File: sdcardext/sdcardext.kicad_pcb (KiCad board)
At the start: 2 copper layers, 2 parts, among them J1 Micro_SD_Card_Det2

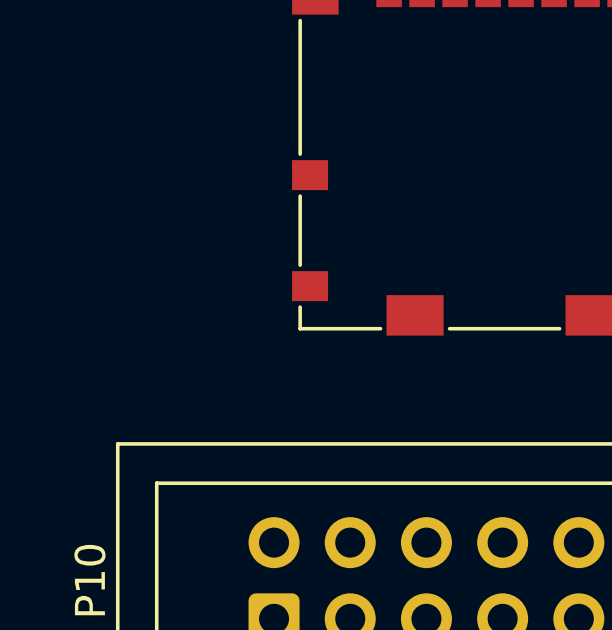
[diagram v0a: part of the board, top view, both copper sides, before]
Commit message: add part#, pullup for CD
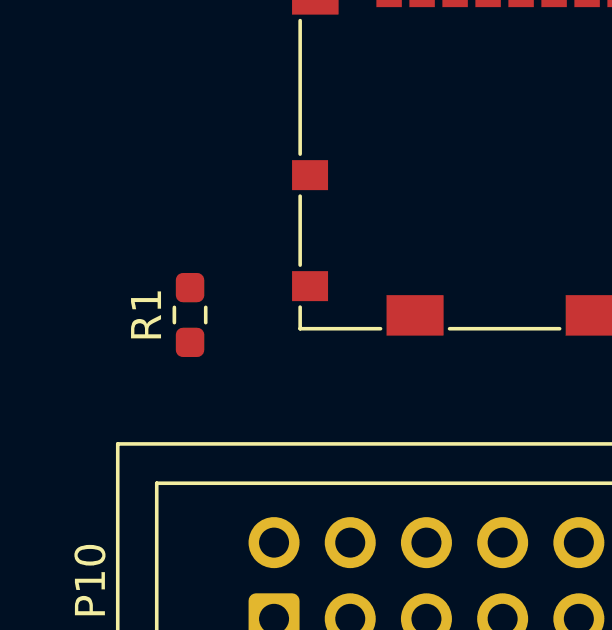
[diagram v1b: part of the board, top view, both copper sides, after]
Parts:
- added R1: 10k, Resistor_SMD:R_0603_1608Metric_Pad0.98x0.95mm_HandSolder, F.Cu at (90.5, 70.7)
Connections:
- J1 pad 10: unconnected-(J1-DET_A-Pad10) -> Net-(J1-DET_A)
- J1 pad 9: unconnected-(J1-DET_B-Pad9) -> Net-(J1-DET_A)
- P10 pad 6: unconnected-(P10-CD-Pad6) -> Net-(J1-DET_A)
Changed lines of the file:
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@@
 	(net 1 "Net-(J1-CMD)")
 	(net 2 "Net-(J1-DAT1)")
-	(net 3 "unconnected-(J1-DET_B-Pad9)")
+	(net 3 "Net-(J1-DET_A)")
 	(net 4 "Net-(J1-CLK)")
 	(net 5 "Net-(J1-DAT3{slash}CD)")
@@
 	(net 8 "VCC")
 	(net 9 "Net-(J1-DAT2)")
-	(net 10 "unconnected-(P10-CD-Pad6)")
-	(net 11 "unconnected-(J1-SHIELD-Pad11)")
-	(net 12 "unconnected-(J1-DET_A-Pad10)")
+	(net 10 "unconnected-(J1-SHIELD-Pad11)")
 	(footprint "Connector_Card:microSD_HC_Molex_104031-0811"
 		(layer "F.Cu")
@@
 			)
 		)
+		(property "LCSC" "C585350"
+			(at 0 0 0)
+			(layer "F.SilkS")
+			(hide yes)
+			(effects
+				(font
+					(size 1.27 1.27)
+					(thickness 0.15)
+				)
+			)
+		)
 		(property ki_fp_filters "microSD*")
 		(sheetname "/")
@@
 			(size 1.2 1)
 			(layers "F.Cu" "F.Mask" "F.Paste")
-			(net 3 "unconnected-(J1-DET_B-Pad9)")
+			(net 3 "Net-(J1-DET_A)")
 			(pinfunction "DET_B")
 			(pintype "passive")
@@
 			(size 1.2 1)
 			(layers "F.Cu" "F.Mask" "F.Paste")
-			(net 12 "unconnected-(J1-DET_A-Pad10)")
+			(net 3 "Net-(J1-DET_A)")
 			(pinfunction "DET_A")
 			(pintype "passive")
@@
 			(size 1.55 1.35)
 			(layers "F.Cu" "F.Mask" "F.Paste")
-			(net 11 "unconnected-(J1-SHIELD-Pad11)")
+			(net 10 "unconnected-(J1-SHIELD-Pad11)")
 			(pinfunction "SHIELD")
 			(pintype "passive")
@@
 			(size 1.9 1.35)
 			(layers "F.Cu" "F.Mask" "F.Paste")
-			(net 11 "unconnected-(J1-SHIELD-Pad11)")
+			(net 10 "unconnected-(J1-SHIELD-Pad11)")
 			(pinfunction "SHIELD")
 			(pintype "passive")
@@
 			(size 1.9 1.35)
 			(layers "F.Cu" "F.Mask" "F.Paste")
-			(net 11 "unconnected-(J1-SHIELD-Pad11)")
+			(net 10 "unconnected-(J1-SHIELD-Pad11)")
 			(pinfunction "SHIELD")
 			(pintype "passive")
@@
 			(size 1.17 1.8)
 			(layers "F.Cu" "F.Mask" "F.Paste")
-			(net 11 "unconnected-(J1-SHIELD-Pad11)")
+			(net 10 "unconnected-(J1-SHIELD-Pad11)")
 			(pinfunction "SHIELD")
 			(pintype "passive")
@@
 			(layers "*.Cu" "*.Mask")
 			(remove_unused_layers no)
-			(net 10 "unconnected-(P10-CD-Pad6)")
+			(net 3 "Net-(J1-DET_A)")
 			(pinfunction "CD")
 			(pintype "output")
@@
 			(offset
 				(xyz 0 0 0)
+			)
+			(scale
+				(xyz 1 1 1)
+			)
+			(rotate
+				(xyz 0 0 0)
+			)
+		)
+	)
+	(footprint "Resistor_SMD:R_0603_1608Metric_Pad0.98x0.95mm_HandSolder"
+		(layer "F.Cu")
+		(at 90.5 70.6625 90)
+		(descr "Resistor SMD 0603 (1608 Metric), square (rectangular) end terminal, IPC-7351 nominal with elongated pad for handsoldering. (Body size source: IPC-SM-782 page 72, https://www.pcb-3d.com/wordpress/wp-content/uploads/ipc-sm-782a_amendment_1_and_2.pdf), generated with kicad-footprint-generator")
+		(tags "resistor handsolder")
+		(property "Reference" "R1"
+			(at 0 -1.43 90)
+			(layer "F.SilkS")
+			(effects
+				(font
+					(size 1 1)
+					(thickness 0.15)
+				)
+			)
+		)
+		(property "Value" "10k"
+			(at 0 1.43 90)
+			(layer "F.Fab")
+			(effects
+				(font
+					(size 1 1)
+					(thickness 0.15)
+				)
+			)
+		)
+		(property "Datasheet" "~"
+			(at 0 0 90)
+			(layer "F.Fab")
+			(hide yes)
+			(effects
+				(font
+					(size 1.27 1.27)
+					(thickness 0.15)
+				)
+			)
+		)
+		(property "Description" "Resistor"
+			(at 0 0 90)
+			(layer "F.Fab")
+			(hide yes)
+			(effects
+				(font
+					(size 1.27 1.27)
+					(thickness 0.15)
+				)
+			)
+		)
+		(property ki_fp_filters "R_*")
+		(sheetname "/")
+		(sheetfile "sdcardext.kicad_sch")
+		(attr smd)
+		(fp_line
+			(start -0.254724 -0.5225)
+			(end 0.254724 -0.5225)
+			(stroke
+				(width 0.12)
+				(type solid)
+			)
+			(layer "F.SilkS")
+		)
+		(fp_line
+			(start -0.254724 0.5225)
+			(end 0.254724 0.5225)
+			(stroke
+				(width 0.12)
+				(type solid)
+			)
+			(layer "F.SilkS")
+		)
+		(fp_line
+			(start 1.65 -0.73)
+			(end 1.65 0.73)
+			(stroke
+				(width 0.05)
+				(type solid)
+			)
+			(layer "F.CrtYd")
+		)
+		(fp_line
+			(start -1.65 -0.73)
+			(end 1.65 -0.73)
+			(stroke
+				(width 0.05)
+				(type solid)
+			)
+			(layer "F.CrtYd")
+		)
+		(fp_line
+			(start 1.65 0.73)
+			(end -1.65 0.73)
+			(stroke
+				(width 0.05)
+				(type solid)
+			)
+			(layer "F.CrtYd")
+		)
+		(fp_line
+			(start -1.65 0.73)
+			(end -1.65 -0.73)
+			(stroke
+				(width 0.05)
+				(type solid)
+			)
+			(layer "F.CrtYd")
+		)
+		(fp_line
+			(start 0.8 -0.4125)
+			(end 0.8 0.4125)
+			(stroke
+				(width 0.1)
+				(type solid)
+			)
+			(layer "F.Fab")
+		)
+		(fp_line
+			(start -0.8 -0.4125)
+			(end 0.8 -0.4125)
+			(stroke
+				(width 0.1)
+				(type solid)
+			)
+			(layer "F.Fab")
+		)
+		(fp_line
+			(start 0.8 0.4125)
+			(end -0.8 0.4125)
+			(stroke
+				(width 0.1)
+				(type solid)
+			)
+			(layer "F.Fab")
+		)
+		(fp_line
+			(start -0.8 0.4125)
+			(end -0.8 -0.4125)
+			(stroke
+				(width 0.1)
+				(type solid)
+			)
+			(layer "F.Fab")
+		)
+		(fp_text user "${REFERENCE}"
+			(at 0 0 90)
+			(layer "F.Fab")
+			(effects
+				(font
+					(size 0.4 0.4)
+					(thickness 0.06)
+				)
+			)
+		)
+		(pad "1" smd roundrect
+			(at -0.9125 0 90)
+			(size 0.975 0.95)
+			(layers "F.Cu" "F.Mask" "F.Paste")
+			(roundrect_rratio 0.25)
+			(net 8 "VCC")
+			(pintype "passive")
+		)
+		(pad "2" smd roundrect
+			(at 0.9125 0 90)
+			(size 0.975 0.95)
+			(layers "F.Cu" "F.Mask" "F.Paste")
+			(roundrect_rratio 0.25)
+			(net 3 "Net-(J1-DET_A)")
+			(pintype "passive")
+		)
+		(embedded_fonts no)
+		(model "${KICAD9_3DMODEL_DIR}/Resistor_SMD.3dshapes/R_0603_1608Metric.step"
+			(offset
+				(xyz 0 0 0)

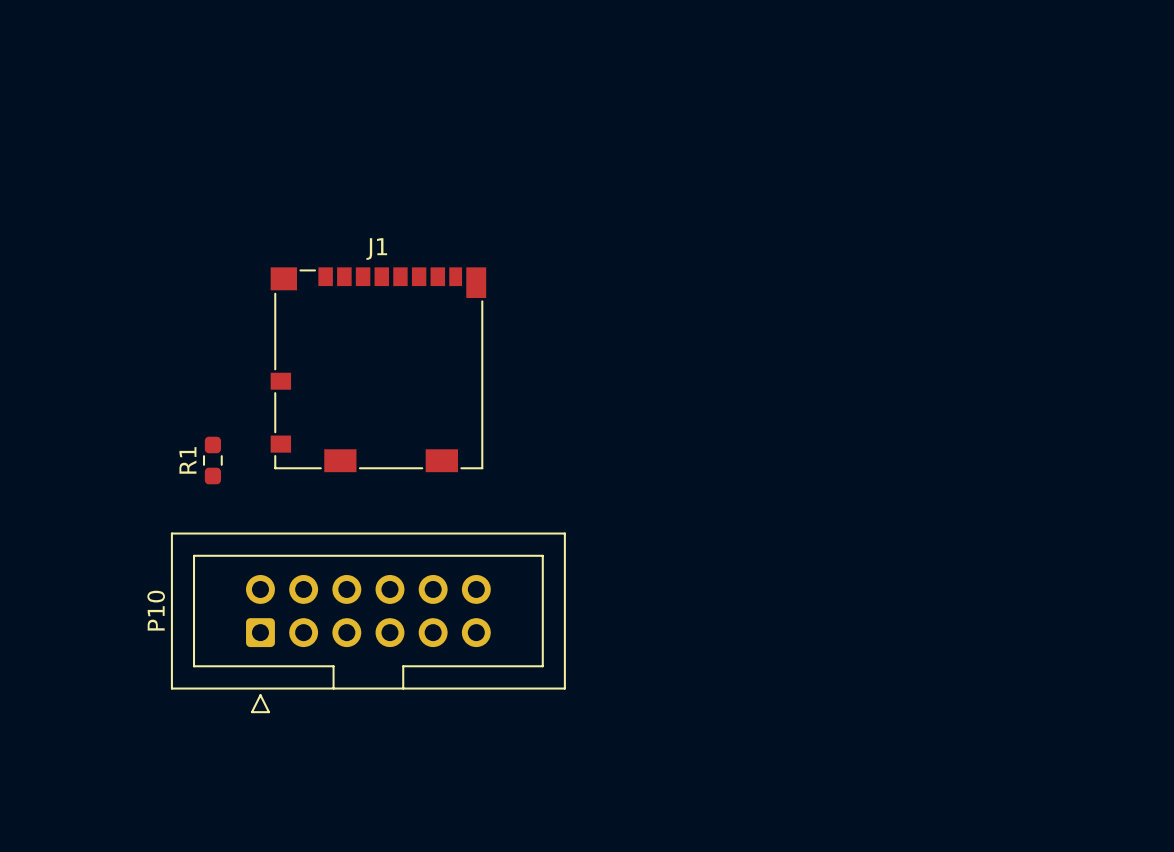
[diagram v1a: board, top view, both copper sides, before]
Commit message: SD card and volumn poti test extension
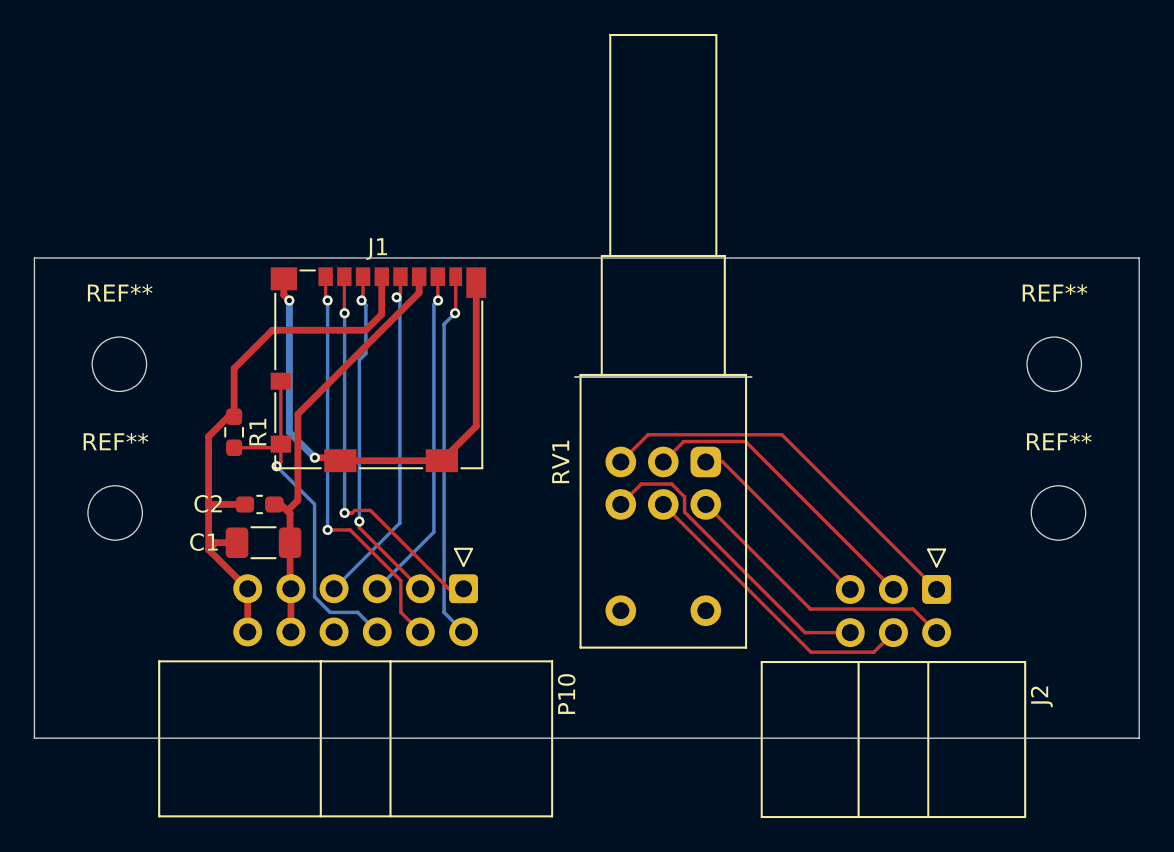
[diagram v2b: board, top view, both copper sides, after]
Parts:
- added C1: 100u, Capacitor_SMD:C_1206_3216Metric_Pad1.33x1.80mm_HandSolder, F.Cu at (93.5, 75.5)
- added C2: 100n, Capacitor_SMD:C_0603_1608Metric_Pad1.08x0.95mm_HandSolder, F.Cu at (93.2, 73.2)
- added J2: Conn_02x03_Odd_Even, Connector_IDC:IDC-Header_2x03_P2.54mm_Horizontal, F.Cu at (133.1, 78.2)
- added REF**: MountingHole_3.2mm_M3, MountingHole:MountingHole_3.2mm_M3, F.Cu at (140.0, 65.0)
- added REF**: MountingHole_3.2mm_M3, MountingHole:MountingHole_3.2mm_M3, F.Cu at (84.8, 73.8)
- added REF**: MountingHole_3.2mm_M3, MountingHole:MountingHole_3.2mm_M3, F.Cu at (140.2, 73.8)
- added REF**: MountingHole_3.2mm_M3, MountingHole:MountingHole_3.2mm_M3, F.Cu at (85.0, 65.0)
- added RV1: R_Potentiometer_Dual, Potentiometer_THT:Potentiometer_Alps_RK097_Dual_Horizontal_Switch, F.Cu at (119.5, 70.8)
- P10: footprint Connector_IDC:IDC-Header_2x06_P2.54mm_Vertical -> Connector_IDC:IDC-Header_2x06_P2.54mm_Horizontal
- moved P10 12.2 mm to (105.2, 78.2), turned to -90 degrees
- moved R1 2.08 mm to (91.8, 69.0), turned to -90 degrees
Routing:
- net VCC: track 0.00 -> 33.5 mm
- net unconnected-(J1-SHIELD-Pad11): track 0.00 -> 30.1 mm, vias 0 -> 2
- net GNDD: track 0.00 -> 25.1 mm
- net Net-(J1-DAT2): track 0.00 -> 24.0 mm, vias 0 -> 2
- net Net-(J2-Pin_1): track 0.00 -> 23.0 mm
- net Net-(J1-DAT3/CD): track 0.00 -> 22.9 mm, vias 0 -> 2
- net Net-(J1-DAT1): track 0.00 -> 21.7 mm, vias 0 -> 1
- net Net-(J1-DET_A): track 0.00 -> 21.1 mm, vias 0 -> 1
- net Net-(J1-CMD): track 0.00 -> 20.1 mm, vias 0 -> 2
- net Net-(J1-CLK): track 0.00 -> 20.1 mm, vias 0 -> 1
- net Net-(J1-DAT0): track 0.00 -> 19.8 mm, vias 0 -> 1
- net Net-(J2-Pin_6): track 0.00 -> 18.1 mm
- net Net-(J2-Pin_3): track 0.00 -> 17.6 mm
- net Net-(J2-Pin_4): track 0.00 -> 17.6 mm
- net Net-(J2-Pin_2): track 0.00 -> 16.7 mm
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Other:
- board outline added: 65 x 28.2 mm
